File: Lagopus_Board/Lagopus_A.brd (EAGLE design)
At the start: 88.9 x 71.2 mm, 39 parts, among them J1 PTH, J2 PTH, U1 MLX90614_, U2 VL53L1X, U3 APDS-9301, U5 AS72652, U6 AS72651, U7 AS72653, U8 MX25L4006E

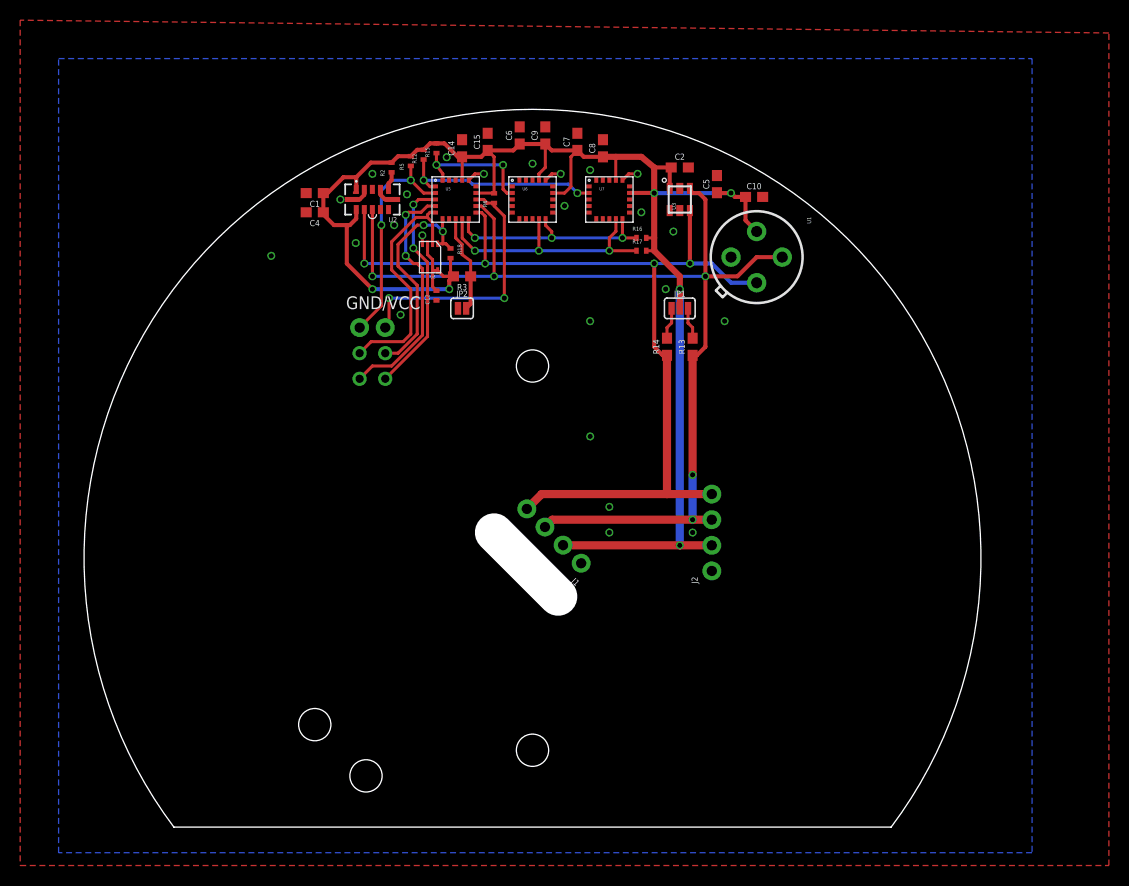
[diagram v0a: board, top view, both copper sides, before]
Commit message: Ordered Version 1.0 from Seeed
Lemming_SMD V1.0
Lagopus_A V1.0
Lagopus_B V1.0
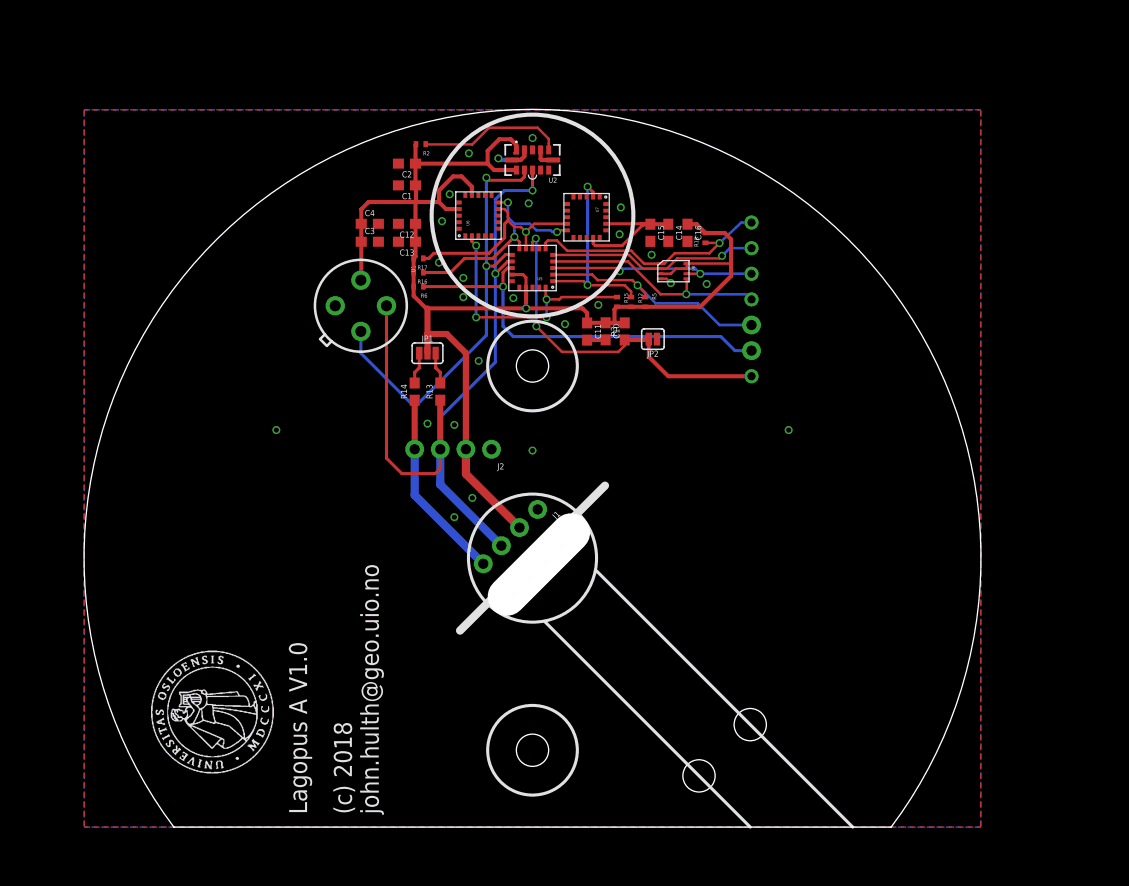
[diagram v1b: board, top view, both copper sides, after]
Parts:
- removed C5, C8, C9: 10uF, SparkFun-Capacitors:0603
- removed C6, C7: 1.0uF, SparkFun-Capacitors:0603
- removed U3: APDS-9301, SparkFun-Sensors:CHIPLED-6
- added C11, C13, C16: 1.0uF, SparkFun-Capacitors:0603
- added C3: 10uF, SparkFun-Capacitors:0603
- added U$4: HN01, PWSONN6:HN01
- added U$5: (no value), UIO-John:UIO-LOGO-BL
- C10: value 0.1uF -> 10uF
- C12: value 1 uF -> 10uF; device Spark:C0402_B -> SparkFun-Capacitors:0603
- C14: value 1.0uF -> 10uF
- C15: value 10uF -> 1.0uF
- moved U$8 40.2 mm to (21.7, 30.7)
- moved U$1 39.7 mm to (21.7, 25.7)
- moved U1 39.5 mm to (-17.0, 25.0)
- moved GND/VCC 38.9 mm to (21.7, 23.1), turned to 270 degrees
- moved U$7 38.6 mm to (21.7, 33.3)
- moved U$2 37.8 mm to (21.7, 28.2)
- moved R5 27.1 mm to (11.2, 25.4), turned to 270 degrees
- moved C2 27.1 mm to (-12.4, 39.1), turned to 180 degrees
- moved JP1 25.4 mm to (-10.4, 20.3)
- moved R13 25.4 mm to (-9.14, 16.5)
- moved R14 25.4 mm to (-11.7, 16.5)
- moved R18 25.3 mm to (17.1, 31.8), turned to 90 degrees
- moved R12 25.2 mm to (9.78, 25.4), turned to 270 degrees
- moved J2 25.0 mm to (-4.06, 10.8), turned to 180 degrees
- moved U8 24.2 mm to (14.0, 28.4), turned to 270 degrees
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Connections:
- net 3.3V: now also C11.1, C12.1, C13.1, C16.1, C3.1; no longer C12.2, C5.1, C6.1, C7.1, C8.1, C9.1, U3.P1
- net GND: now also C11.2, C12.2, C13.2, C16.2, C3.2; no longer C12.1, C5.2, C6.2, C7.2, C8.2, C9.2, U3.P2
- net I2C_EN: now also U$4.P$1
- net SCL: no longer U3.P4
- net SDA: no longer U3.P5
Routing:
- net SDA: track 107.5 -> 75.4 mm, vias 5 -> 2
- net SCL: track 98.7 -> 67.0 mm, vias 4 -> 2
- net I2C_EN: track 9.74 -> 35.9 mm, vias 0 -> 2
- net 3.3V: track 169.2 -> 153.5 mm, vias 6 -> 1
- net !INT: track 26.3 -> 39.9 mm, vias 2 -> 1
- net !SHUT: track 1.82 -> 14.4 mm
- net SLV2_RESN: track 13.0 -> 25.3 mm, vias 2 -> 4
- net SCL_M: track 26.3 -> 21.0 mm, vias 3 -> 1
- net SO: track 24.3 -> 21.1 mm, vias 0 -> 1
- net !CS: track 23.1 -> 25.1 mm, vias 2 -> 1
- net GND: track 10.1 -> 8.39 mm, vias 24 -> 25
- net SI: track 24.2 -> 22.8 mm, vias 2 -> 1
- net !RST: track 22.2 -> 23.2 mm, vias 2 -> 1
- net SLV1_RESN: track 20.4 -> 19.7 mm
- net SCK: track 22.0 -> 21.4 mm
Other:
- outline, holes or cut-outs redrawn
- board text added: "(c) 2018 john.hulth@geo.uio.no"
- board text added: "Lagopus A V1.0"
